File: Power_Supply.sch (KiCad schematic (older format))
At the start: 64 parts, among them Q1 FDS9926A, U5 ADP5052ACPZ-R7

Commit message: Added new sheet for Ethernet PHY Connector and drawn schematic (continue)
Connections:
- net at U5.12 (BST4): now also C19.1
- net at U5.3 (SW3): now also C18.2, L3.2
- net at U5.45 (FB3): now also R19.2
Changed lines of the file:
@@
 $Descr A4 11693 8268
 encoding utf-8
-Sheet 13 14
+Sheet 13 15
 Title ""
 Date ""

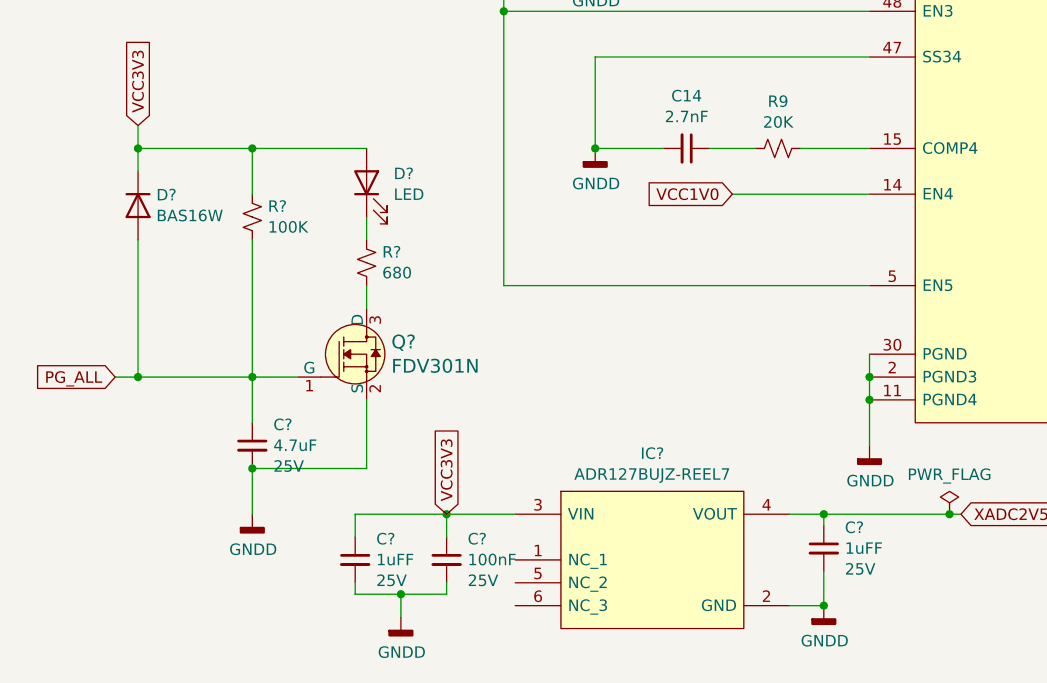
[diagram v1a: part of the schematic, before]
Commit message: Added USB SRAM sheet,Added USB3 ethernet ic
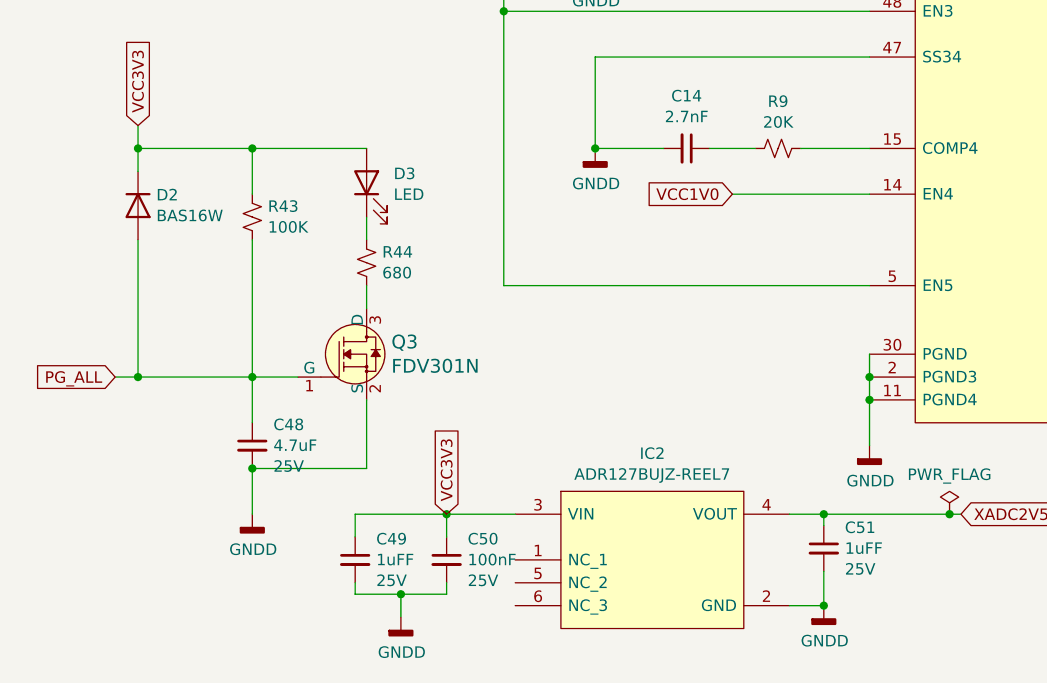
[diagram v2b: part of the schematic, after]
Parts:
- gave numbers to parts that had none: 10
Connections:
- net at U5.12 (BST4): now also C19.1
- net at U5.3 (SW3): now also C18.2, L3.2
- net at U5.45 (FB3): now also R19.2
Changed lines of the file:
@@
 $Descr A4 11693 8268
 encoding utf-8
-Sheet 13 15
+Sheet 16 17
 Title ""
 Date ""
@@
 PG_ALL
 $Comp
-L Diode:BAS16W D?
+L Diode:BAS16W D2
 U 1 1 603E6DD0
 P 1100 5750
-F 0 "D?" V 1054 5830 50  0000 L CNN
+F 0 "D2" V 1054 5830 50  0000 L CNN
 F 1 "BAS16W" V 1145 5830 50  0000 L CNN
 F 2 "Package_TO_SOT_SMD:SOT-323_SC-70" H 1100 5575 50  0001 C CNN
@@
 $EndComp
 $Comp
-L dk_Transistors-FETs-MOSFETs-Single:FDV301N Q?
+L dk_Transistors-FETs-MOSFETs-Single:FDV301N Q3
 U 1 1 603E9366
 P 2100 6400
-F 0 "Q?" H 2208 6453 60  0000 L CNN
+F 0 "Q3" H 2208 6453 60  0000 L CNN
 F 1 "FDV301N" H 2208 6347 60  0000 L CNN
 F 2 "digikey-footprints:SOT-23-3" H 2300 6600 60  0001 L CNN
@@
 $EndComp
 $Comp
-L Device:R_Small_US R?
+L Device:R_Small_US R43
 U 1 1 603F4D4F
 P 1600 5800
-F 0 "R?" H 1532 5754 50  0000 R CNN
+F 0 "R43" H 1532 5754 50  0000 R CNN
 F 1 "100K" H 1532 5845 50  0000 R CNN
 F 2 "Resistor_SMD:R_0603_1608Metric_Pad0.98x0.95mm_HandSolder" H 1600 5800 50  0001 C CNN
@@
 Connection ~ 1600 6500
 $Comp
-L Device:LED D?
+L Device:LED D3
 U 1 1 6043B321
 P 2100 5650
-F 0 "D?" V 2139 5532 50  0000 R CNN
+F 0 "D3" V 2139 5532 50  0000 R CNN
 F 1 "LED" V 2048 5532 50  0000 R CNN
 F 2 "LED_SMD:LED_0603_1608Metric_Pad1.05x0.95mm_HandSolder" H 2100 5650 50  0001 C CNN
@@
 $EndComp
 $Comp
-L Device:R_Small_US R?
+L Device:R_Small_US R44
 U 1 1 6043D83F
 P 2100 6000
-F 0 "R?" H 2032 5954 50  0000 R CNN
+F 0 "R44" H 2032 5954 50  0000 R CNN
 F 1 "680" H 2032 6045 50  0000 R CNN
 F 2 "Resistor_SMD:R_0603_1608Metric_Pad0.98x0.95mm_HandSolder" H 2100 6000 50  0001 C CNN
@@
 	2100 6100 2100 6200
 $Comp
-L Device:C_Small C?
+L Device:C_Small C48
 U 1 1 6046D604
 P 1600 6800
-F 0 "C?" H 1692 6891 50  0000 L CNN
+F 0 "C48" H 1692 6891 50  0000 L CNN
 F 1 "4.7uF" H 1692 6800 50  0000 L CNN
 F 2 "Capacitor_SMD:C_0603_1608Metric_Pad1.08x0.95mm_HandSolder" H 1600 6800 50  0001 C CNN
@@
 	2100 6900 1600 6900
 $Comp
-L power:GNDD #PWR?
+L power:GNDD #PWR035
 U 1 1 60487DC4
 P 1600 7100
-F 0 "#PWR?" H 1600 6850 50  0001 C CNN
+F 0 "#PWR035" H 1600 6850 50  0001 C CNN
 F 1 "GNDD" H 1604 6945 50  0000 C CNN
 F 2 "" H 1600 7100 50  0001 C CNN
@@
 47uF - GRM21BR60J476ME15\n22uF - GRM219R61A226MEA0\n1uH - XAL6030-102\n3.3uH - XAL6030-332\n6.8uH - XAL6060-682
 $Comp
-L GM_Voltage_Regulators:ADR127BUJZ-REEL7 IC?
+L GM_Voltage_Regulators:ADR127BUJZ-REEL7 IC2
 U 1 1 604B738E
 P 2950 7000
-F 0 "IC?" H 3350 7165 50  0000 C CNN
+F 0 "IC2" H 3350 7165 50  0000 C CNN
 F 1 "ADR127BUJZ-REEL7" H 3350 7074 50  0000 C CNN
 F 2 "SOT95P280X100-6N" H 4100 7200 50  0001 L CNN
@@
 $EndComp
 $Comp
-L Device:C_Small C?
+L Device:C_Small C50
 U 1 1 604BA563
 P 2450 7300
-F 0 "C?" H 2542 7391 50  0000 L CNN
+F 0 "C50" H 2542 7391 50  0000 L CNN
 F 1 "100nF" H 2542 7300 50  0000 L CNN
 F 2 "Capacitor_SMD:C_0603_1608Metric_Pad1.08x0.95mm_HandSolder" H 2450 7300 50  0001 C CNN
@@
 $EndComp
 $Comp
-L Device:C_Small C?
+L Device:C_Small C49
 U 1 1 604BB8E8
 P 2050 7300
-F 0 "C?" H 2142 7391 50  0000 L CNN
+F 0 "C49" H 2142 7391 50  0000 L CNN
 F 1 "1uFF" H 2142 7300 50  0000 L CNN
 F 2 "Capacitor_SMD:C_0603_1608Metric_Pad1.08x0.95mm_HandSolder" H 2050 7300 50  0001 C CNN
@@
 $EndComp
 $Comp
-L Device:C_Small C?
+L Device:C_Small C51
 U 1 1 604BC582
 P 4100 7250
-F 0 "C?" H 4192 7341 50  0000 L CNN
+F 0 "C51" H 4192 7341 50  0000 L CNN
 F 1 "1uFF" H 4192 7250 50  0000 L CNN
 F 2 "Capacitor_SMD:C_0603_1608Metric_Pad1.08x0.95mm_HandSolder" H 4100 7250 50  0001 C CNN
@@
 	2050 7450 2050 7400
 $Comp
-L power:GNDD #PWR?
+L power:GNDD #PWR036
 U 1 1 604E434D
 P 2250 7550
-F 0 "#PWR?" H 2250 7300 50  0001 C CNN
+F 0 "#PWR036" H 2250 7300 50  0001 C CNN
 F 1 "GNDD" H 2254 7395 50  0000 C CNN
 F 2 "" H 2250 7550 50  0001 C CNN
@@
 	4100 7350 4100 7500
 $Comp
-L power:GNDD #PWR?
+L power:GNDD #PWR037
 U 1 1 6052D71E
 P 4100 7500
-F 0 "#PWR?" H 4100 7250 50  0001 C CNN
+F 0 "#PWR037" H 4100 7250 50  0001 C CNN
 F 1 "GNDD" H 4104 7345 50  0000 C CNN
 F 2 "" H 4100 7500 50  0001 C CNN
@@
 Connection ~ 4100 7500
 $Comp
-L power:PWR_FLAG #FLG?
+L power:PWR_FLAG #FLG020
 U 1 1 6052E9FE
 P 4650 7100
-F 0 "#FLG?" H 4650 7175 50  0001 C CNN
+F 0 "#FLG020" H 4650 7175 50  0001 C CNN
 F 1 "PWR_FLAG" H 4650 7273 50  0000 C CNN
 F 2 "" H 4650 7100 50  0001 C CNN

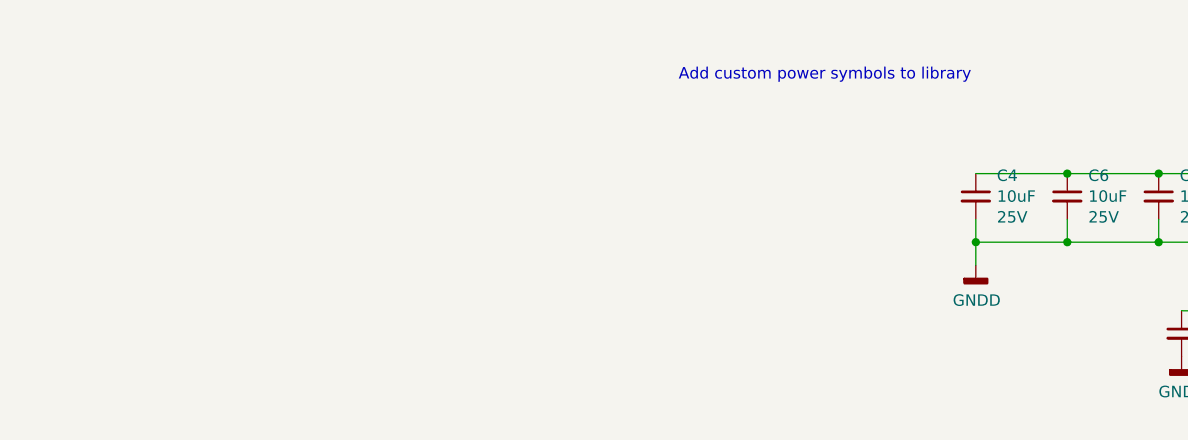
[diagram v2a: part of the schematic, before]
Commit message: Completed power 48v to 12v sheet
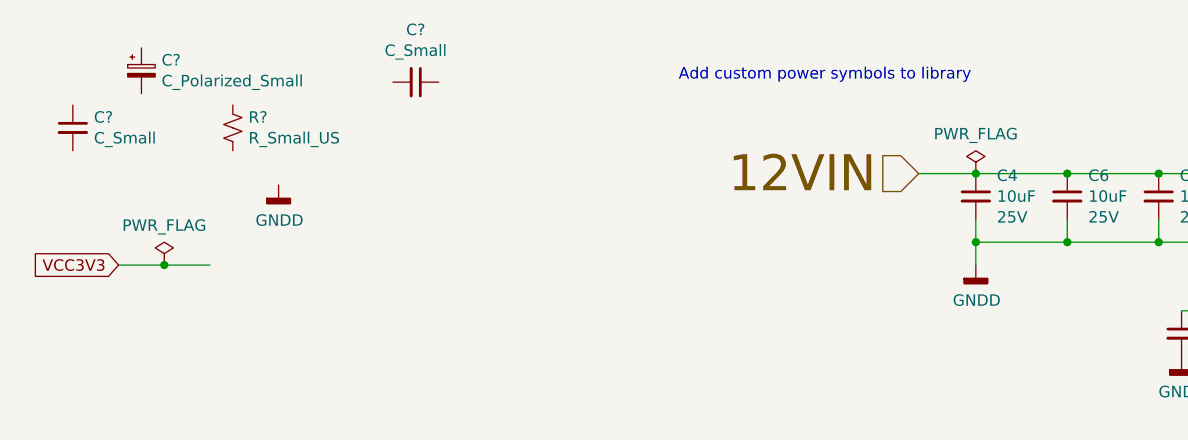
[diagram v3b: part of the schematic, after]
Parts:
- added C?: C_Small, Capacitor_SMD:C_0603_1608Metric_Pad1.08x0.95mm_HandSolder, symbol Device:C_Small
- added C?: C_Polarized_Small, Capacitor_Tantalum_SMD:CP_EIA-1608-10_AVX-L_Pad1.25x1.05mm_HandSolder, symbol Device:C_Polarized_Small
- added C?: C_Small, symbol Device:C_Small
- added R?: R_Small_US, Resistor_SMD:R_0603_1608Metric_Pad0.98x0.95mm_HandSolder, symbol Device:R_Small_US
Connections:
- net at U5.12 (BST4): now also C19.1
- net 12VIN: now reaches C4.1, C6.1, C7.1, C9.1, U5.24 (PVIN2_1), U5.25 (PVIN2_2), U5.35 (PVIN1_1), U5.36 (PVIN1_2), U5.4 (PVIN3), U5.9 (PVIN4)
- net at U5.3 (SW3): now also C18.2, L3.2
- net at U5.45 (FB3): now also R19.2
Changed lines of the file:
@@
 Wire Wire Line
 	4650 7100 4700 7100
+Text HLabel 1650 1000 0    157  Input ~ 0
+12VIN
+Wire Wire Line
+	1900 1000 1650 1000
+Connection ~ 1900 1000
+$Comp
+L power:PWR_FLAG #FLG?
+U 1 1 602F5542
+P 1900 1000
+F 0 "#FLG?" H 1900 1075 50  0001 C CNN
+F 1 "PWR_FLAG" H 1900 1173 50  0000 C CNN
+F 2 "" H 1900 1000 50  0001 C CNN
+F 3 "~" H 1900 1000 50  0001 C CNN
+	1    1900 1000
+	1    0    0    -1
+$EndComp
+$Comp
+L Device:R_Small_US R?
+U 1 1 603121C7
+P -1350 800
+AR Path="/601E7C5A/603121C7" Ref="R?"  Part="1"
+AR Path="/601E7CC8/603121C7" Ref="R?"  Part="1"
+AR Path="/601E7C92/603121C7" Ref="R?"  Part="1"
+AR Path="/601E7C92/60257FE5/603121C7" Ref="R?"  Part="1"
+AR Path="/601E7B38/603121C7" Ref="R?"  Part="1"
+AR Path="/601DF0A6/603121C7" Ref="R?"  Part="1"
+F 0 "R?" H -1282 846 50  0000 L CNN
+F 1 "R_Small_US" H -1282 755 50  0000 L CNN
+F 2 "Resistor_SMD:R_0603_1608Metric_Pad0.98x0.95mm_HandSolder" H -1350 800 50  0001 C CNN
+F 3 "~" H -1350 800 50  0001 C CNN
+	1    -1350 800
+	1    0    0    -1
+$EndComp
+$Comp
+L Device:C_Small C?
+U 1 1 603121CE
+P -2050 800
+AR Path="/601E7C5A/603121CE" Ref="C?"  Part="1"
+AR Path="/601E7CC8/603121CE" Ref="C?"  Part="1"
+AR Path="/601E7C92/603121CE" Ref="C?"  Part="1"
+AR Path="/601E7C92/60257FE5/603121CE" Ref="C?"  Part="1"
+AR Path="/601E7B38/603121CE" Ref="C?"  Part="1"
+AR Path="/601DF0A6/603121CE" Ref="C?"  Part="1"
+F 0 "C?" H -1958 846 50  0000 L CNN
+F 1 "C_Small" H -1958 755 50  0000 L CNN
+F 2 "Capacitor_SMD:C_0603_1608Metric_Pad1.08x0.95mm_HandSolder" H -2050 800 50  0001 C CNN
+F 3 "~" H -2050 800 50  0001 C CNN
+F 4 "" H -2050 800 50  0000 C CNN "Voltage"
+	1    -2050 800
+	1    0    0    -1
+$EndComp
+Text GLabel -1850 1400 0    50   Input ~ 0
+VCC3V3
+$Comp
+L power:PWR_FLAG #FLG?
+U 1 1 603121D5
+P -1650 1400
+AR Path="/601E7C5A/603121D5" Ref="#FLG?"  Part="1"
+AR Path="/601E7CC8/603121D5" Ref="#FLG?"  Part="1"
+AR Path="/601E7C92/603121D5" Ref="#FLG?"  Part="1"
+AR Path="/601E7C92/60257FE5/603121D5" Ref="#FLG?"  Part="1"
+AR Path="/601E7B38/603121D5" Ref="#FLG?"  Part="1"
+AR Path="/601DF0A6/603121D5" Ref="#FLG?"  Part="1"
+F 0 "#FLG?" H -1650 1475 50  0001 C CNN
+F 1 "PWR_FLAG" H -1650 1573 50  0000 C CNN
+F 2 "" H -1650 1400 50  0001 C CNN
+F 3 "~" H -1650 1400 50  0001 C CNN
+	1    -1650 1400
+	1    0    0    -1
+$EndComp
+Connection ~ -1650 1400
+Wire Wire Line
+	-1650 1400 -1450 1400
+Wire Wire Line
+	-1850 1400 -1650 1400
+$Comp
+L power:GNDD #PWR?
+U 1 1 603121DE
+P -1150 1050
+AR Path="/601DF0A6/603121DE" Ref="#PWR?"  Part="1"
+AR Path="/601E7C5A/603121DE" Ref="#PWR?"  Part="1"
+AR Path="/601E7CC8/603121DE" Ref="#PWR?"  Part="1"
+AR Path="/601E7C92/603121DE" Ref="#PWR?"  Part="1"
+AR Path="/601E7C92/60257FE5/603121DE" Ref="#PWR?"  Part="1"
+AR Path="/601E7B38/603121DE" Ref="#PWR?"  Part="1"
+F 0 "#PWR?" H -1150 800 50  0001 C CNN
+F 1 "GNDD" H -1146 895 50  0000 C CNN
+F 2 "" H -1150 1050 50  0001 C CNN
+F 3 "" H -1150 1050 50  0001 C CNN
+	1    -1150 1050
+	1    0    0    -1
+$EndComp
+$Comp
+L Device:C_Polarized_Small C?
+U 1 1 603121E5
+P -1750 550
+AR Path="/601E7C92/603121E5" Ref="C?"  Part="1"
+AR Path="/601E7C92/60257FE5/603121E5" Ref="C?"  Part="1"
+AR Path="/601E7B38/603121E5" Ref="C?"  Part="1"
+AR Path="/601DF0A6/603121E5" Ref="C?"  Part="1"
+F 0 "C?" H -1662 596 50  0000 L CNN
+F 1 "C_Polarized_Small" H -1662 505 50  0000 L CNN
+F 2 "Capacitor_Tantalum_SMD:CP_EIA-1608-10_AVX-L_Pad1.25x1.05mm_HandSolder" H -1750 550 50  0001 C CNN
+F 3 "~" H -1750 550 50  0001 C CNN
+F 4 "" H -1750 550 50  0000 C CNN "Voltage"
+	1    -1750 550
+	1    0    0    -1
+$EndComp
+$Comp
+L Device:C_Small C?
+U 1 1 603121EB
+P -550 600
+AR Path="/601E7B38/603121EB" Ref="C?"  Part="1"
+AR Path="/601DF0A6/603121EB" Ref="C?"  Part="1"
+F 0 "C?" V -779 600 50  0000 C CNN
+F 1 "C_Small" V -688 600 50  0000 C CNN
+F 2 "" H -550 600 50  0001 C CNN
+F 3 "~" H -550 600 50  0001 C CNN
+	1    -550 600
+	0    1    1    0
+$EndComp
 $EndSCHEMATC

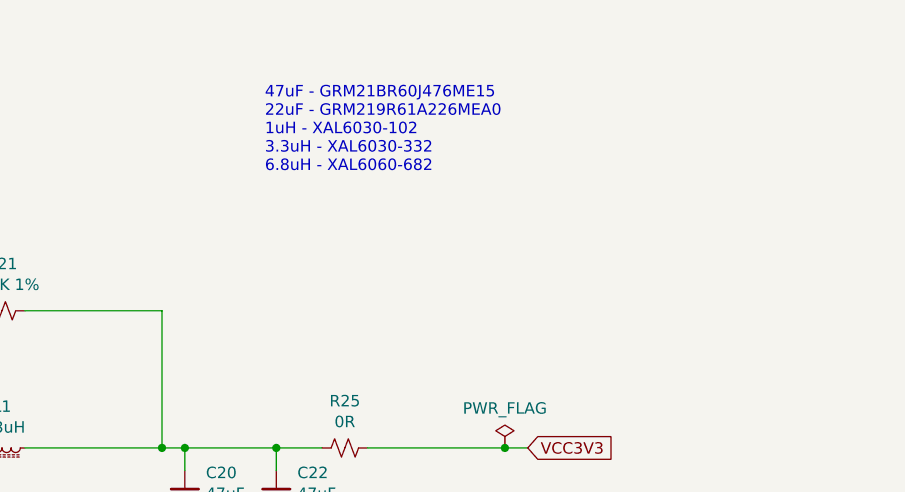
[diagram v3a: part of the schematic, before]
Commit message: Completed USB3 1.2V Added 5V regulator cct partially completed Added BTB connector
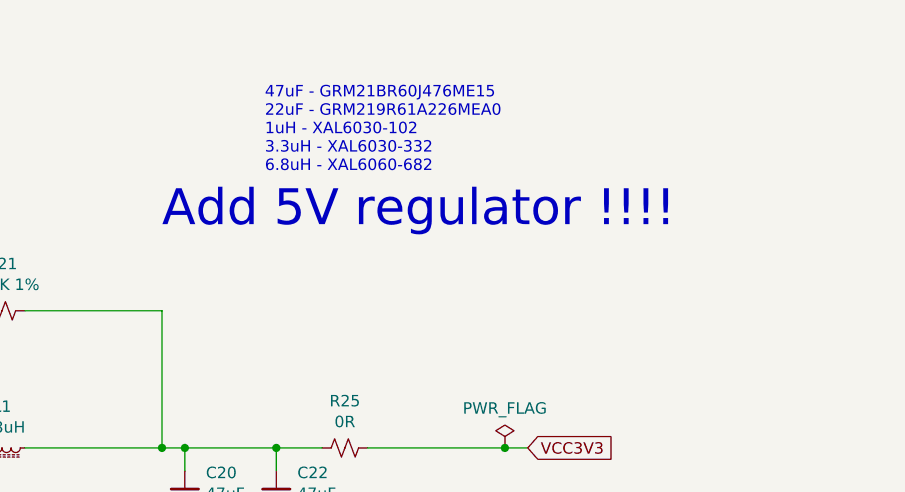
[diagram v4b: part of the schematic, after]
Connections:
- net at U5.12 (BST4): now also C19.1
- net at U5.3 (SW3): now also C18.2, L3.2
- net at U5.45 (FB3): now also R19.2
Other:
- note added: "Add 5V regulator !!!!"
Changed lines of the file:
@@
 $Descr A4 11693 8268
 encoding utf-8
-Sheet 16 17
+Sheet 16 18
 Title ""
 Date ""
@@
 	0    1    1    0
 $EndComp
+Text Notes 8500 1250 0    157  ~ 0
+Add 5V regulator !!!!
 $EndSCHEMATC

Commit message: Added USB3 SRAM Added 5V regulator
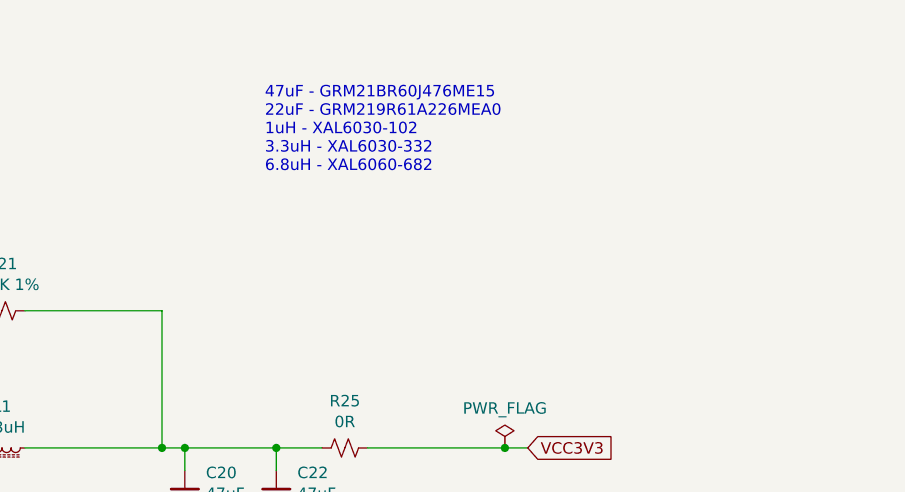
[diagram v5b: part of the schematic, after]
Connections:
- net at U5.12 (BST4): now also C19.1
- net at U5.3 (SW3): now also C18.2, L3.2
- net at U5.45 (FB3): now also R19.2
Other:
- note removed: "Add 5V regulator !!!!"
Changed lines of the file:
@@
 	0    1    1    0
 $EndComp
-Text Notes 8500 1250 0    157  ~ 0
-Add 5V regulator !!!!
 $EndSCHEMATC

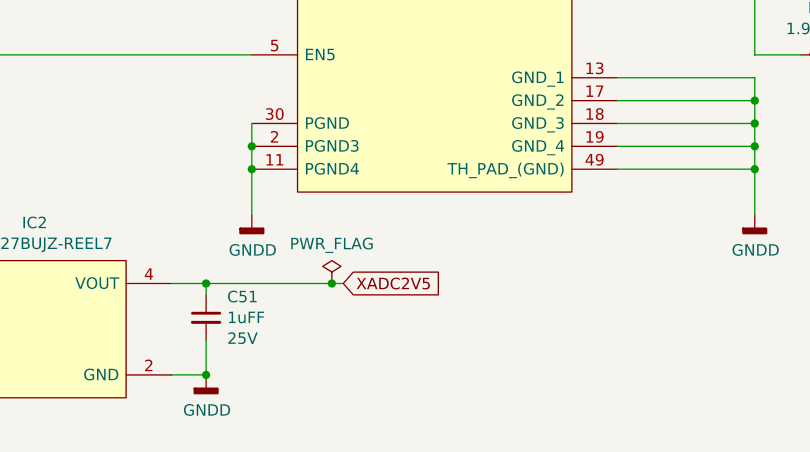
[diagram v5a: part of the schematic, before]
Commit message: Completed FPGA power sheet completed USB3 completed FPGA config
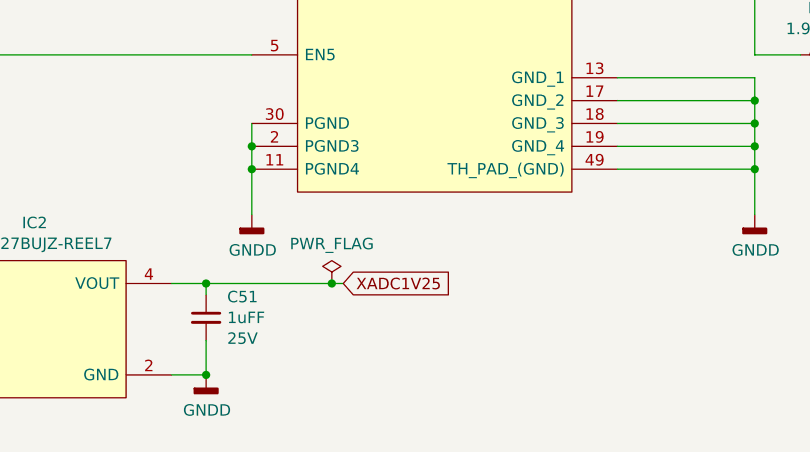
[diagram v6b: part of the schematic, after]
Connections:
- net at U5.12 (BST4): now also C19.1
- net at U5.3 (SW3): now also C18.2, L3.2
- net at U5.45 (FB3): now also R19.2
- net XADC2V5 renamed XADC1V25
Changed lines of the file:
@@
 VCC3V3
 Text GLabel 4700 7100 2    50   Input ~ 0
-XADC2V5
+XADC1V25
 Wire Wire Line
 	3950 7100 4100 7100

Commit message: Added sheet Ext_Analog
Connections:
- net at U5.12 (BST4): now also C19.1
- net at U5.3 (SW3): now also C18.2, L3.2
- net at U5.45 (FB3): now also R19.2

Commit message: Completed LED_Comm Completed Ext_Analog Added AWG and ADC sheets
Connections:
- net at U5.12 (BST4): now also C19.1
- net at U5.3 (SW3): now also C18.2, L3.2
- net at U5.45 (FB3): now also R19.2
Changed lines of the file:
@@
 $Descr A4 11693 8268
 encoding utf-8
-Sheet 13 18
+Sheet 13 19
 Title ""
 Date ""
